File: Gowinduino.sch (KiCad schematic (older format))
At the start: 13 parts, among them J1 Power, J2 Analog, J3 Digital, J4 Digital, J5 SPI, U1 GW1NSR-4CQN48P, U2 W25Q32JVSS

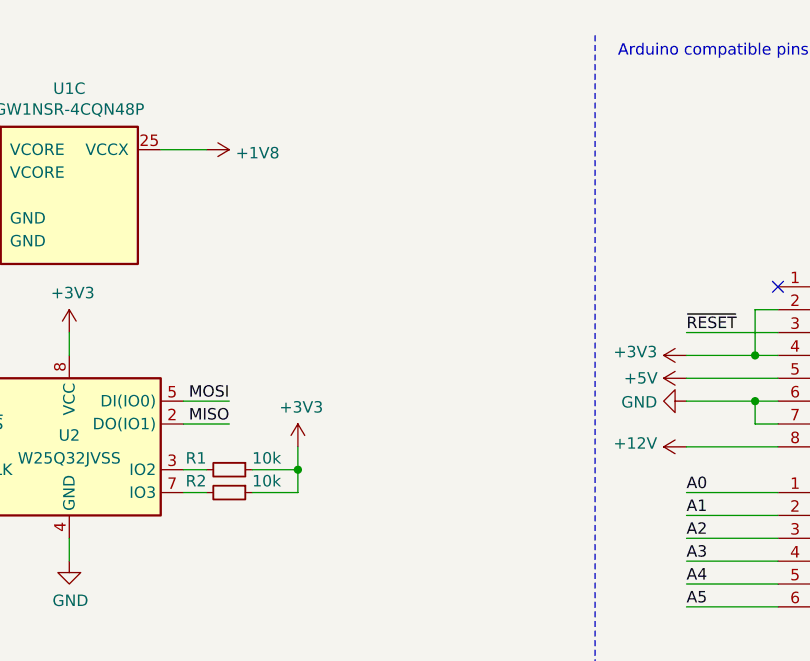
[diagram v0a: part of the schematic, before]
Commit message: PCB: Hooking up the JTAG port.
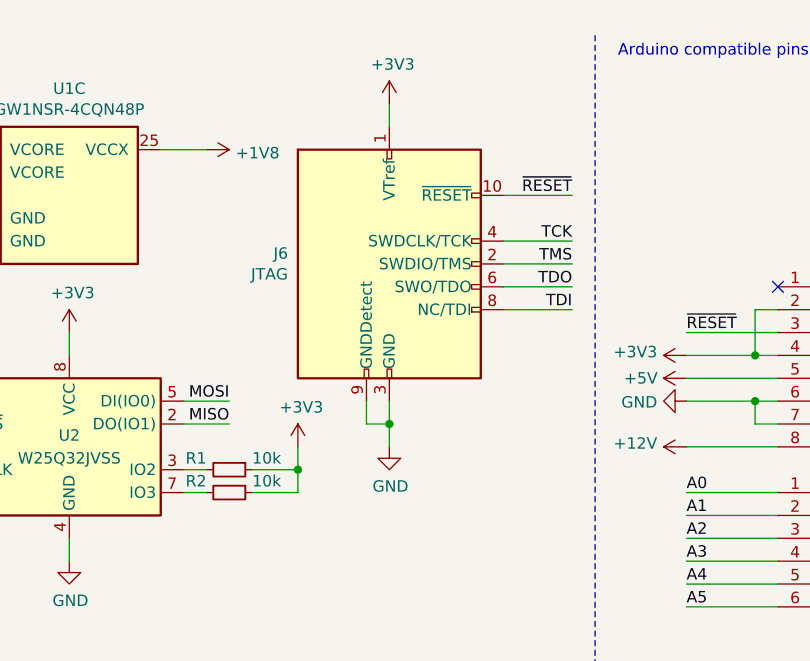
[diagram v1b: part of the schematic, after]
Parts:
- added J6: JTAG, Connector_PinHeader_1.27mm:PinHeader_2x05_P1.27mm_Vertical, symbol Connector:Conn_ARM_JTAG_SWD_10
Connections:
- net +3V3: now also J6.1 (VTref)
- net GND: now also J6.3 (GND), J6.5 (GND), J6.9 (GNDDetect)
- net TCK: now also J6.4 (SWDCLK/TCK)
- net TDI: now also J6.8 (NC/TDI)
- net TDO: now also J6.6 (SWO/TDO)
- net TMS: now also J6.2 (SWDIO/TMS)
- net ~RESET: now also J6.10 (~RESET~)
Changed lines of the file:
@@
 Wire Wire Line
 	6000 2400 6200 2400
+$Comp
+L Connector:Conn_ARM_JTAG_SWD_10 J6
+U 1 1 60860373
+P 8100 1500
+F 0 "J6" H 7657 1546 50  0000 R CNN
+F 1 "JTAG" H 7657 1455 50  0000 R CNN
+F 2 "Connector_PinHeader_1.27mm:PinHeader_2x05_P1.27mm_Vertical" H 8100 1500 50  0001 C CNN
+F 3 "http://infocenter.arm.com/help/topic/com.arm.doc.ddi0314h/DDI0314H_coresight_components_trm.pdf" V 7750 250 50  0001 C CNN
+	1    8100 1500
+	1    0    0    -1
+$EndComp
+$Comp
+L power:+3V3 #PWR0117
+U 1 1 60863F1F
+P 8100 800
+F 0 "#PWR0117" H 8100 650 50  0001 C CNN
+F 1 "+3V3" H 8115 973 50  0000 C CNN
+F 2 "" H 8100 800 50  0001 C CNN
+F 3 "" H 8100 800 50  0001 C CNN
+	1    8100 800
+	1    0    0    -1
+$EndComp
+$Comp
+L power:GND #PWR0118
+U 1 1 608644AF
+P 8100 2300
+F 0 "#PWR0118" H 8100 2050 50  0001 C CNN
+F 1 "GND" H 8105 2127 50  0000 C CNN
+F 2 "" H 8100 2300 50  0001 C CNN
+F 3 "" H 8100 2300 50  0001 C CNN
+	1    8100 2300
+	1    0    0    -1
+$EndComp
+Wire Wire Line
+	8100 2100 8100 2200
+Wire Wire Line
+	8100 2200 8000 2200
+Wire Wire Line
+	8000 2200 8000 2100
+Connection ~ 8100 2200
+Wire Wire Line
+	8100 2200 8100 2300
+Wire Wire Line
+	8100 800  8100 900
+Text Label 8900 1200 2    50   ~ 0
+~RESET
+Text Label 8900 1400 2    50   ~ 0
+TCK
+Text Label 8900 1500 2    50   ~ 0
+TMS
+Text Label 8900 1600 2    50   ~ 0
+TDO
+Text Label 8900 1700 2    50   ~ 0
+TDI
+Wire Wire Line
+	8900 1200 8600 1200
+Wire Wire Line
+	8600 1400 8900 1400
+Wire Wire Line
+	8900 1500 8600 1500
+Wire Wire Line
+	8600 1600 8900 1600
+Wire Wire Line
+	8900 1700 8600 1700
 $EndSCHEMATC

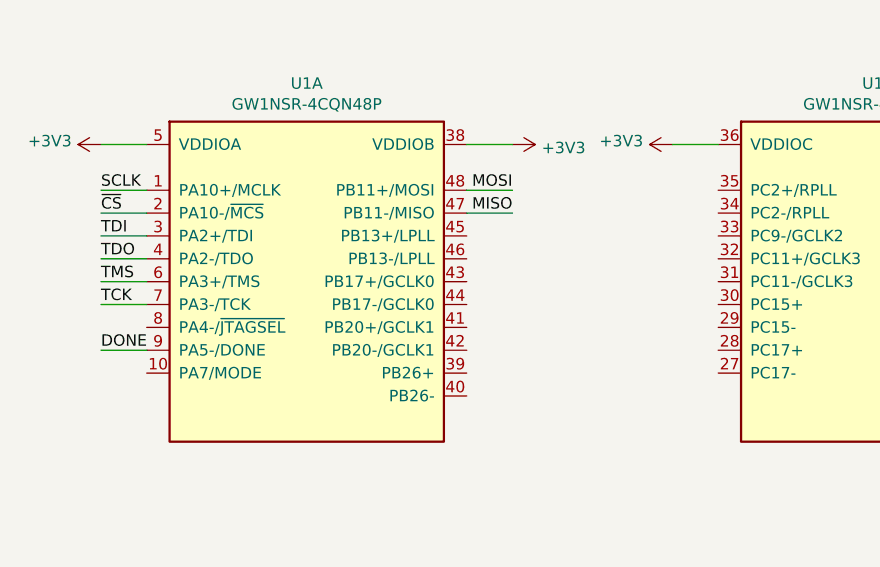
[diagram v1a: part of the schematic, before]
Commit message: PCB: Hookup all 3.3V IO pins
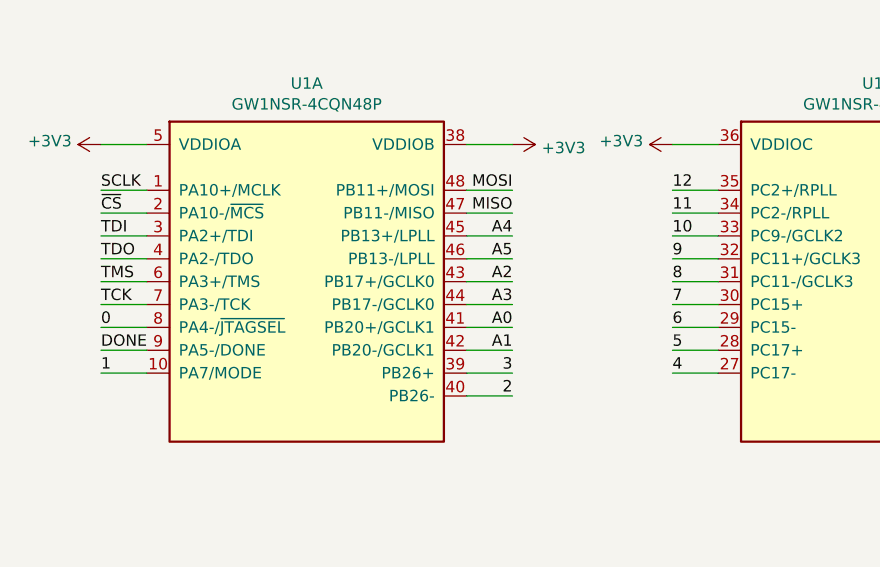
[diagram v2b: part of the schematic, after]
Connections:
- net 0: now also U1.8 (PA4-/~JTAGSEL)
- net 1: now also U1.10 (PA7/MODE)
- net 10: now also U1.33 (PC9-/GCLK2)
- net 11: now also U1.34 (PC2-/RPLL)
- net 12: now also U1.35 (PC2+/RPLL)
- net 2: now also U1.40 (PB26-)
- net 3: now also U1.39 (PB26+)
- net 4: now also U1.27 (PC17-)
- net 5: now also U1.28 (PC17+)
- net 6: now also U1.29 (PC15-)
- net 7: now also U1.30 (PC15+)
- net 8: now also U1.31 (PC11-/GCLK3)
- net 9: now also U1.32 (PC11+/GCLK3)
- net A0: now also U1.41 (PB20+/GCLK1)
- net A1: now also U1.42 (PB20-/GCLK1)
- net A2: now also U1.43 (PB17+/GCLK0)
- net A3: now also U1.44 (PB17-/GCLK0)
- net A4: now also U1.45 (PB13+/LPLL)
- net A5: now also U1.46 (PB13-/LPLL)
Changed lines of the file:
@@
 Wire Wire Line
 	8900 1700 8600 1700
+Text Label 1100 1800 0    50   ~ 0
+0
+Text Label 1100 2000 0    50   ~ 0
+1
+Wire Wire Line
+	1100 2000 1300 2000
+Wire Wire Line
+	1100 1800 1300 1800
+Text Label 2900 1400 2    50   ~ 0
+A4
+Text Label 2900 1500 2    50   ~ 0
+A5
+Text Label 2900 1600 2    50   ~ 0
+A2
+Text Label 2900 1700 2    50   ~ 0
+A3
+Text Label 2900 1800 2    50   ~ 0
+A0
+Text Label 2900 1900 2    50   ~ 0
+A1
+Wire Wire Line
+	2900 1400 2700 1400
+Wire Wire Line
+	2700 1500 2900 1500
+Wire Wire Line
+	2900 1600 2700 1600
+Wire Wire Line
+	2700 1700 2900 1700
+Wire Wire Line
+	2900 1800 2700 1800
+Wire Wire Line
+	2700 1900 2900 1900
+Text Label 2900 2100 2    50   ~ 0
+2
+Text Label 2900 2000 2    50   ~ 0
+3
+Wire Wire Line
+	2900 2000 2700 2000
+Wire Wire Line
+	2700 2100 2900 2100
+Text Label 3600 2000 0    50   ~ 0
+4
+Text Label 3600 1900 0    50   ~ 0
+5
+Text Label 3600 1800 0    50   ~ 0
+6
+Text Label 3600 1700 0    50   ~ 0
+7
+Text Label 3600 1600 0    50   ~ 0
+8
+Text Label 3600 1500 0    50   ~ 0
+9
+Text Label 3600 1400 0    50   ~ 0
+10
+Text Label 3600 1300 0    50   ~ 0
+11
+Text Label 3600 1200 0    50   ~ 0
+12
+Wire Wire Line
+	3600 1200 3800 1200
+Wire Wire Line
+	3800 1300 3600 1300
+Wire Wire Line
+	3600 1400 3800 1400
+Wire Wire Line
+	3800 1500 3600 1500
+Wire Wire Line
+	3600 1600 3800 1600
+Wire Wire Line
+	3800 1700 3600 1700
+Wire Wire Line
+	3600 1800 3800 1800
+Wire Wire Line
+	3800 1900 3600 1900
+Wire Wire Line
+	3600 2000 3800 2000
 $EndSCHEMATC

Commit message: Implemented the 1.8V conversion out
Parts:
- added C1, C2, C3, C4, C5, C6, C7: 100n, Capacitor_SMD:C_0603_1608Metric_Pad1.08x0.95mm_HandSolder, symbol Device:C_Small
- added U3: TXB0104PW, Package_SO:TSSOP-14_4.4x5mm_P0.65mm, symbol Logic_LevelTranslator:TXB0104PW
- added U4: SN74AVC4T245PW, Package_SO:TSSOP-16_4.4x5mm_P0.65mm, symbol Logic_LevelTranslator:SN74AVC4T245PW
- added U5, U6: SN74LVC1T45DBV, Package_TO_SOT_SMD:SOT-23-6, symbol Logic_LevelTranslator:SN74LVC1T45DBV
- added U7: MAX811SEUS-T, Package_TO_SOT_SMD:SOT-143, symbol Power_Supervisor:MAX811SEUS-T
- added X1: 24M, Oscillator:Oscillator_SMD_EuroQuartz_XO53-4Pin_5.0x3.2mm, symbol Oscillator:XO53
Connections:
- net labels added: CLK24M, L13, L14, L15, LRX, LTX, LU+, LU-, LUEN, LUOE, MCLK, U+, U-, UEN, ~RST
- wire segments 107 -> 215

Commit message: PCB: Wiring up all GPIO pins
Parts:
- removed U4: SN74AVC4T245PW, Package_SO:TSSOP-16_4.4x5mm_P0.65mm, symbol Logic_LevelTranslator:SN74AVC4T245PW
- removed U5, U6: SN74LVC1T45DBV, Package_TO_SOT_SMD:SOT-23-6, symbol Logic_LevelTranslator:SN74LVC1T45DBV
- removed U7: MAX811SEUS-T, Package_TO_SOT_SMD:SOT-143, symbol Power_Supervisor:MAX811SEUS-T
- removed X1: 24M, Oscillator:Oscillator_SMD_EuroQuartz_XO53-4Pin_5.0x3.2mm, symbol Oscillator:XO53
- added C10, C8, C9: 22µ, Capacitor_SMD:C_0805_2012Metric_Pad1.18x1.45mm_HandSolder, symbol Device:C_Small
- added L1, L2: 2.2µH, Inductor_SMD:L_0805_2012Metric_Pad1.15x1.40mm_HandSolder, symbol Device:L_Core_Ferrite_Small
- added R3, R5, R6: 10k, Resistor_SMD:R_0603_1608Metric_Pad0.98x0.95mm_HandSolder, symbol Device:R_Small
- added R4: 20k, Resistor_SMD:R_0603_1608Metric_Pad0.98x0.95mm_HandSolder, symbol Device:R_Small
- added RN1: 220, Resistor_SMD:R_Array_Convex_4x0603, symbol Device:R_Pack04
- added SW1: Mode, Button_Switch_SMD:SW_SPDT_PCM12, symbol Switch:SW_SPDT
- added U4: MP2122, Package_TO_SOT_SMD:SOT-23-8, symbol Regulator_Switching:MP2122
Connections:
- net labels added: JTCK, JTDI, JTDO, JTMS, L12, MODE
- net labels removed: CLK24M, LU+, LU-, LUEN, LUOE, RX, TX, U+, U-, UEN

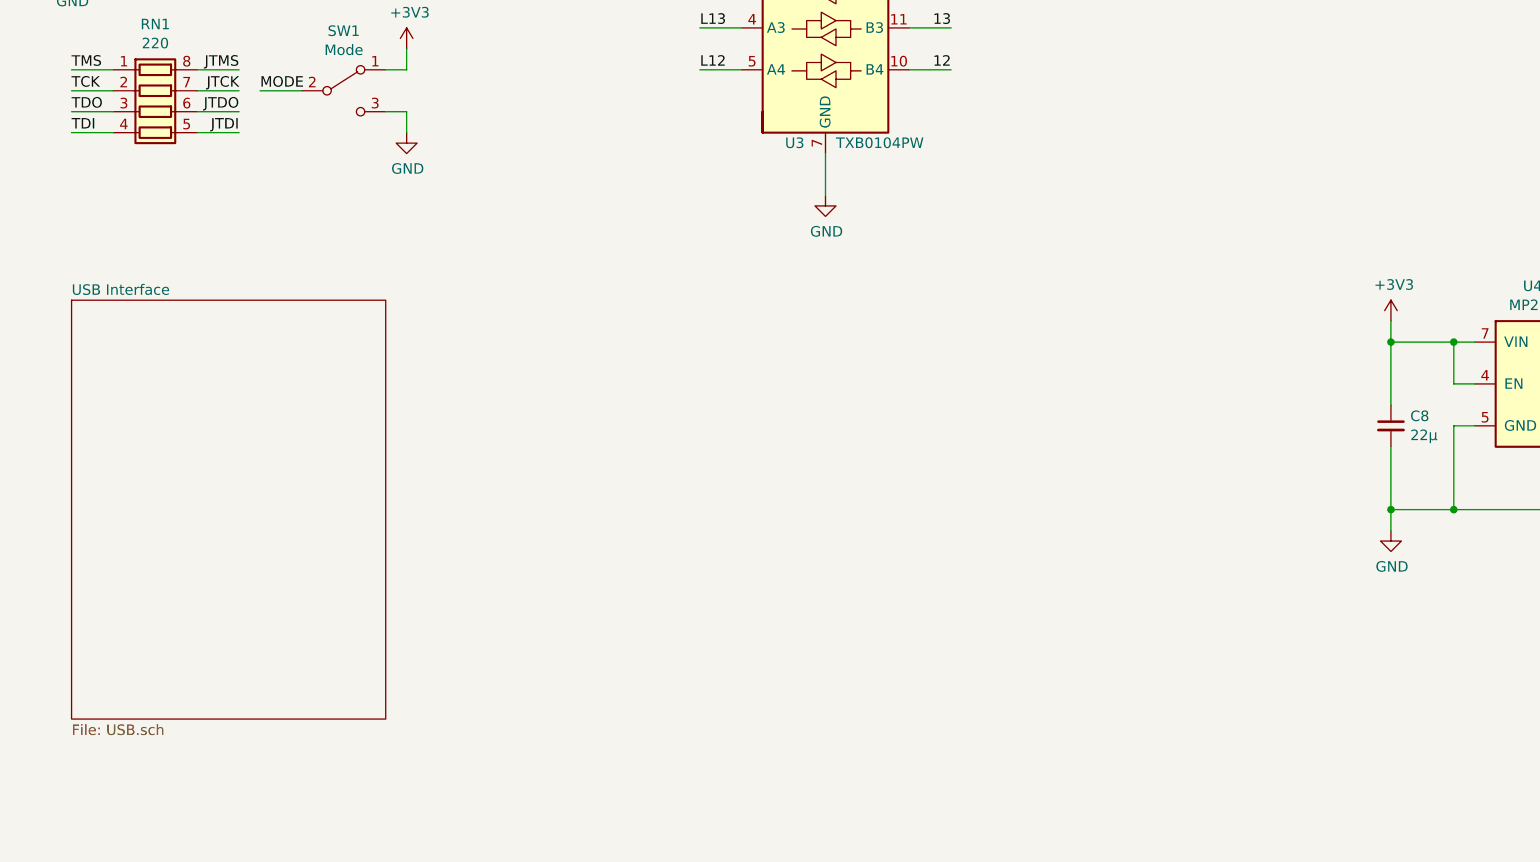
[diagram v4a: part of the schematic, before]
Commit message: Implemented: USB and 12V VIN
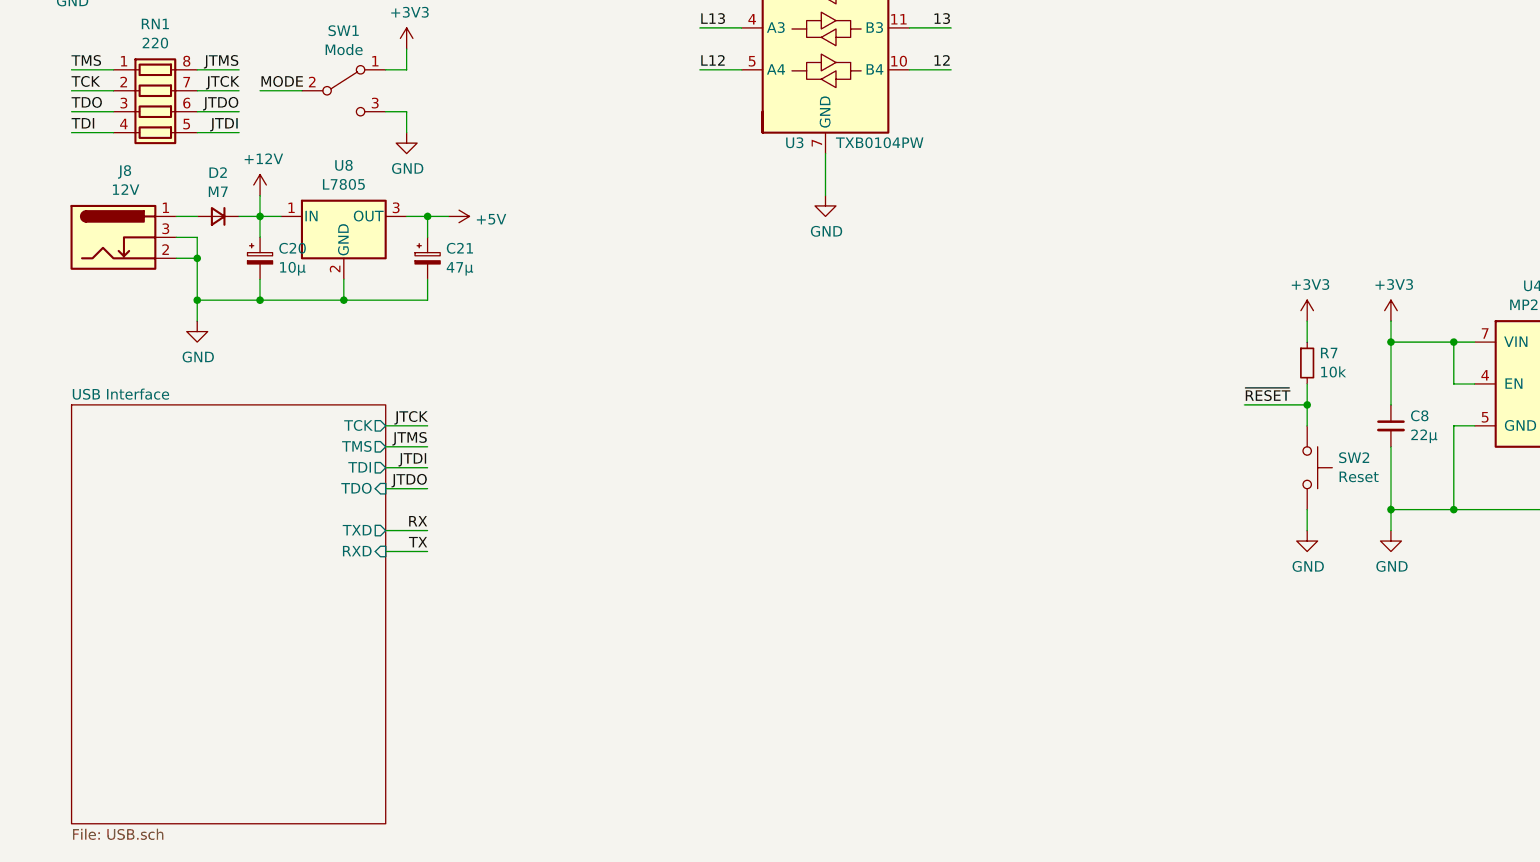
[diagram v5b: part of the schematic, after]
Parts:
- added C20: 10µ, Capacitor_SMD:CP_Elec_4x4.5, symbol Device:CP_Small
- added C21: 47µ, Capacitor_SMD:CP_Elec_4x4.5, symbol Device:CP_Small
- added D2: M7, Diode_SMD:D_SMA, symbol Device:D_Small
- added J8: 12V, Connector_BarrelJack:BarrelJack_Wuerth_6941xx301002, symbol Connector:Barrel_Jack_Switch
- added R7: 10k, Resistor_SMD:R_0603_1608Metric_Pad0.98x0.95mm_HandSolder, symbol Device:R_Small
- added SW2: Reset, Button_Switch_THT:SW_PUSH_6mm, symbol Switch:SW_Push
- added U8: L7805, Package_TO_SOT_SMD:TO-252-2, symbol Regulator_Linear:L7805
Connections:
- net +12V: now also C20.1, D2.1 (K), U8.1 (IN)
- net +3V3: now also R7.1
- net +5V: now also C21.1, U8.3 (OUT)
- net GND: now also C20.2, C21.2, J8.2, J8.3, SW2.2, U8.2 (GND)
- net ~RESET: now also R7.2, SW2.1
- new net: D2.2 (A), J8.1
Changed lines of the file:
@@
 $Descr A4 11693 8268
 encoding utf-8
-Sheet 1 1
+Sheet 1 2
 Title ""
 Date "lun. 30 mars 2015"
@@
 $EndComp
 $Sheet
-S 1000 5000 1500 2000
+S 1000 5500 1500 2000
 U 60B8EB7D
 F0 "USB Interface" 50
 F1 "USB.sch" 50
+F2 "TCK" O R 2500 5600 50
+F3 "TDI" O R 2500 5800 50
+F4 "TDO" I R 2500 5900 50
+F5 "TMS" O R 2500 5700 50
+F6 "TXD" O R 2500 6100 50
+F7 "RXD" I R 2500 6200 50
 $EndSheet
+$Comp
+L Device:R_Small R7
+U 1 1 60B94904
+P 6900 5300
+F 0 "R7" H 6959 5346 50  0000 L CNN
+F 1 "10k" H 6959 5255 50  0000 L CNN
+F 2 "Resistor_SMD:R_0603_1608Metric_Pad0.98x0.95mm_HandSolder" H 6900 5300 50  0001 C CNN
+F 3 "~" H 6900 5300 50  0001 C CNN
+	1    6900 5300
+	1    0    0    -1
+$EndComp
+$Comp
+L Switch:SW_Push SW2
+U 1 1 60B95D37
+P 6900 5800
+F 0 "SW2" V 6854 5948 50  0000 L CNN
+F 1 "Reset" V 6945 5948 50  0000 L CNN
+F 2 "Button_Switch_THT:SW_PUSH_6mm" H 6900 6000 50  0001 C CNN
+F 3 "~" H 6900 6000 50  0001 C CNN
+	1    6900 5800
+	0    1    1    0
+$EndComp
+$Comp
+L power:+3V3 #PWR0134
+U 1 1 60BA7526
+P 6900 5100
+F 0 "#PWR0134" H 6900 4950 50  0001 C CNN
+F 1 "+3V3" H 6915 5273 50  0000 C CNN
+F 2 "" H 6900 5100 50  0001 C CNN
+F 3 "" H 6900 5100 50  0001 C CNN
+	1    6900 5100
+	1    0    0    -1
+$EndComp
+$Comp
+L power:GND #PWR0135
+U 1 1 60BA7E1E
+P 6900 6100
+F 0 "#PWR0135" H 6900 5850 50  0001 C CNN
+F 1 "GND" H 6905 5927 50  0000 C CNN
+F 2 "" H 6900 6100 50  0001 C CNN
+F 3 "" H 6900 6100 50  0001 C CNN
+	1    6900 6100
+	1    0    0    -1
+$EndComp
+Text Label 6600 5500 0    50   ~ 0
+~RESET
+Wire Wire Line
+	6900 5100 6900 5200
+Wire Wire Line
+	6900 5400 6900 5500
+Wire Wire Line
+	6900 6000 6900 6100
+Wire Wire Line
+	6600 5500 6900 5500
+Connection ~ 6900 5500
+Wire Wire Line
+	6900 5500 6900 5600
+Text Label 2700 5600 2    50   ~ 0
+JTCK
+Text Label 2700 5700 2    50   ~ 0
+JTMS
+Text Label 2700 5800 2    50   ~ 0
+JTDI
+Text Label 2700 5900 2    50   ~ 0
+JTDO
+Text Label 2700 6200 2    50   ~ 0
+TX
+Text Label 2700 6100 2    50   ~ 0
+RX
+Wire Wire Line
+	2700 5600 2500 5600
+Wire Wire Line
+	2500 5700 2700 5700
+Wire Wire Line
+	2700 5800 2500 5800
+Wire Wire Line
+	2500 5900 2700 5900
+Wire Wire Line
+	2700 6100 2500 6100
+Wire Wire Line
+	2500 6200 2700 6200
+$Comp
+L Connector:Barrel_Jack_Switch J8
+U 1 1 60E12F95
+P 1200 4700
+F 0 "J8" H 1257 5017 50  0000 C CNN
+F 1 "12V" H 1257 4926 50  0000 C CNN
+F 2 "Connector_BarrelJack:BarrelJack_Wuerth_6941xx301002" H 1250 4660 50  0001 C CNN
+F 3 "~" H 1250 4660 50  0001 C CNN
+	1    1200 4700
+	1    0    0    -1
+$EndComp
+$Comp
+L Device:D_Small D2
+U 1 1 60E144A6
+P 1700 4600
+F 0 "D2" H 1700 4807 50  0000 C CNN
+F 1 "M7" H 1700 4716 50  0000 C CNN
+F 2 "Diode_SMD:D_SMA" V 1700 4600 50  0001 C CNN
+F 3 "~" V 1700 4600 50  0001 C CNN
+	1    1700 4600
+	-1   0    0    -1
+$EndComp
+$Comp
+L Regulator_Linear:L7805 U8
+U 1 1 60E15206
+P 2300 4600
+F 0 "U8" H 2300 4842 50  0000 C CNN
+F 1 "L7805" H 2300 4751 50  0000 C CNN
+F 2 "Package_TO_SOT_SMD:TO-252-2" H 2325 4450 50  0001 L CIN
+F 3 "http://www.st.com/content/ccc/resource/technical/document/datasheet/41/4f/b3/b0/12/d4/47/88/CD00000444.pdf/files/CD00000444.pdf/jcr:content/translations/en.CD00000444.pdf" H 2300 4550 50  0001 C CNN
+	1    2300 4600
+	1    0    0    -1
+$EndComp
+$Comp
+L Device:CP_Small C20
+U 1 1 60E16E55
+P 1900 4800
+F 0 "C20" H 1988 4846 50  0000 L CNN
+F 1 "10µ" H 1988 4755 50  0000 L CNN
+F 2 "Capacitor_SMD:CP_Elec_4x4.5" H 1900 4800 50  0001 C CNN
+F 3 "~" H 1900 4800 50  0001 C CNN
+	1    1900 4800
+	1    0    0    -1
+$EndComp
+$Comp
+L power:GND #PWR0152
+U 1 1 60E17F0B
+P 1600 5100
+F 0 "#PWR0152" H 1600 4850 50  0001 C CNN
+F 1 "GND" H 1605 4927 50  0000 C CNN
+F 2 "" H 1600 5100 50  0001 C CNN
+F 3 "" H 1600 5100 50  0001 C CNN
+	1    1600 5100
+	1    0    0    -1
+$EndComp
+$Comp
+L power:+12V #PWR0153
+U 1 1 60E18F98
+P 1900 4500
+F 0 "#PWR0153" H 1900 4350 50  0001 C CNN
+F 1 "+12V" H 1915 4673 50  0000 C CNN
+F 2 "" H 1900 4500 50  0001 C CNN
+F 3 "" H 1900 4500 50  0001 C CNN
+	1    1900 4500
+	1    0    0    -1
+$EndComp
+$Comp
+L power:+5V #PWR0154
+U 1 1 60E1991A
+P 2800 4600
+F 0 "#PWR0154" H 2800 4450 50  0001 C CNN
+F 1 "+5V" V 2815 4728 50  0000 L CNN
+F 2 "" H 2800 4600 50  0001 C CNN
+F 3 "" H 2800 4600 50  0001 C CNN
+	1    2800 4600
+	0    1    1    0
+$EndComp
+$Comp
+L Device:CP_Small C21
+U 1 1 60E1ABAD
+P 2700 4800
+F 0 "C21" H 2788 4846 50  0000 L CNN
+F 1 "47µ" H 2788 4755 50  0000 L CNN
+F 2 "Capacitor_SMD:CP_Elec_4x4.5" H 2700 4800 50  0001 C CNN
+F 3 "~" H 2700 4800 50  0001 C CNN
+	1    2700 4800
+	1    0    0    -1
+$EndComp
+Wire Wire Line
+	1500 4600 1600 4600
+Wire Wire Line
+	1800 4600 1900 4600
+Wire Wire Line
+	1900 4500 1900 4600
+Connection ~ 1900 4600
+Wire Wire Line
+	1900 4600 2000 4600
+Wire Wire Line
+	1900 4600 1900 4700
+Wire Wire Line
+	1500 4700 1600 4700
+Wire Wire Line
+	1600 4700 1600 4800
+Wire Wire Line
+	1500 4800 1600 4800
+Connection ~ 1600 4800
+Wire Wire Line
+	1600 4800 1600 5000
+Wire Wire Line
+	1600 5000 1900 5000
+Wire Wire Line
+	2700 5000 2700 4900
+Connection ~ 1600 5000
+Wire Wire Line
+	1600 5000 1600 5100
+Wire Wire Line
+	2600 4600 2700 4600
+Wire Wire Line
+	2700 4700 2700 4600
+Connection ~ 2700 4600
+Wire Wire Line
+	2700 4600 2800 4600
+Wire Wire Line
+	2300 4900 2300 5000
+Connection ~ 2300 5000
+Wire Wire Line
+	2300 5000 2700 5000
+Wire Wire Line
+	1900 4900 1900 5000
+Connection ~ 1900 5000
+Wire Wire Line
+	1900 5000 2300 5000
 $EndSCHEMATC
